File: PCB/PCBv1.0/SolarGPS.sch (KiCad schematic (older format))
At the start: 64 parts, among them J1 Conn_01x10_Female, J2 Solar1+, J3 GND, J4 Conn_02x05_Odd_Even, J5 Solar2+, J6 GND, J7 Screw_Terminal_01x01, U1 BQ25505, U2 MAX-M10Q, U3 MAX40200AUK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

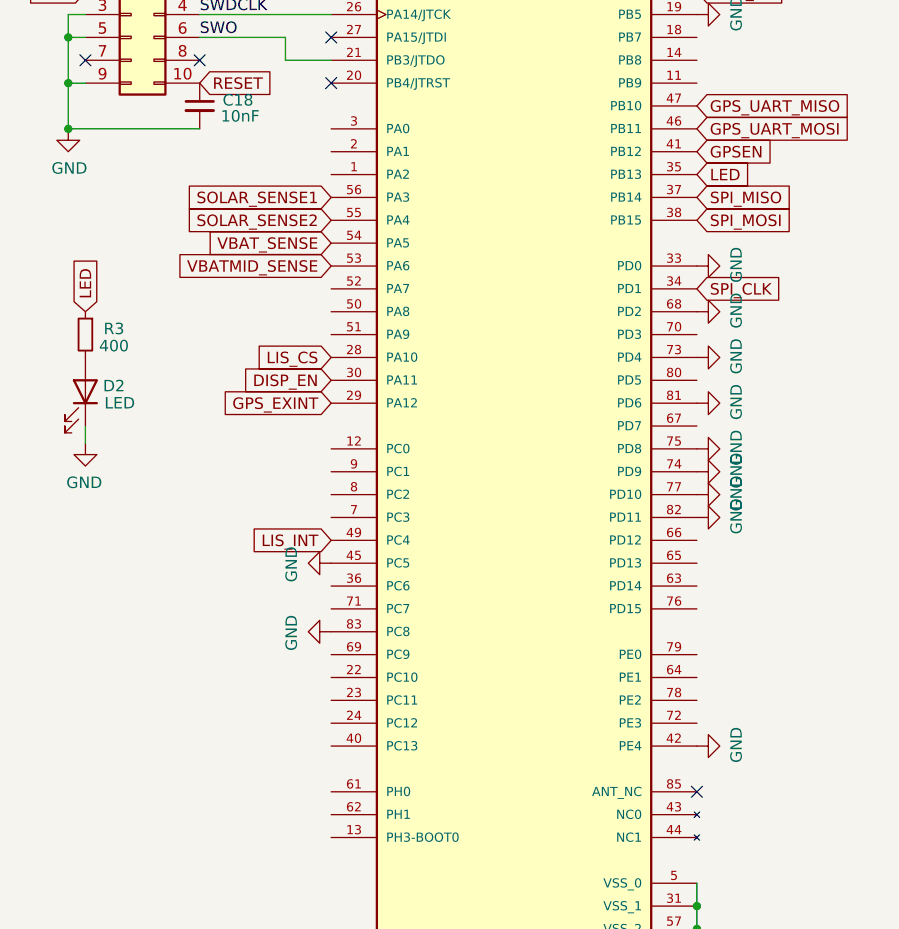
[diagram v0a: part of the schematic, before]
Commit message: Update PCB1.0 with new layout
Reverse the LCD direction for more space on the GPS signal
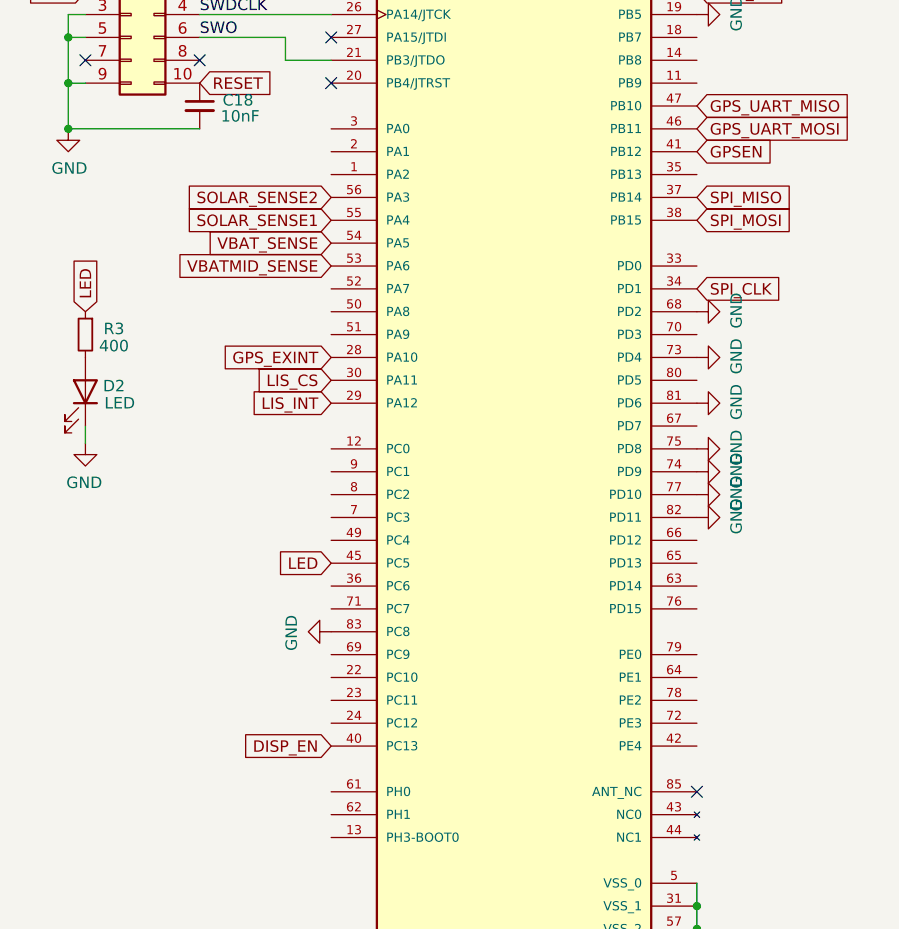
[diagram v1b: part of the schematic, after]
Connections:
- net DISP_EN: now also U4.40 (PC13); no longer U4.30 (PA11)
- net GND: no longer U4.33 (PD0), U4.42 (PE4), U4.45 (PC5)
- net GPS_EXINT: now also U4.28 (PA10); no longer U4.29 (PA12)
- net LED: now also U4.45 (PC5); no longer U4.35 (PB13)
- net LIS_CS: now also U4.30 (PA11); no longer U4.28 (PA10)
- net LIS_INT: now also U4.29 (PA12); no longer U4.49 (PC4)
- net SOLAR_SENSE1: now also U4.55 (PA4); no longer U4.56 (PA3)
- net SOLAR_SENSE2: now also U4.56 (PA3); no longer U4.55 (PA4)
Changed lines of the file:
@@
-$EndComp
-$Comp
-L power:GND #PWR0121
-U 1 1 61AA59EA
-P 10750 4475
-F 0 "#PWR0121" H 10750 4225 50  0001 C CNN
-F 1 "GND" H 10755 4302 50  0000 C CNN
-F 2 "" H 10750 4475 50  0001 C CNN
-F 3 "" H 10750 4475 50  0001 C CNN
-	1    10750 4475
-	0    1    1    0
 $EndComp
 $Comp
@@
 	1    9675 3725
 	0    1    -1   0
-$EndComp
-$Comp
-L power:GND #PWR0118
-U 1 1 61C248C7
-P 12350 2075
-F 0 "#PWR0118" H 12350 1825 50  0001 C CNN
-F 1 "GND" H 12355 1902 50  0000 C CNN
-F 2 "" H 12350 2075 50  0001 C CNN
-F 3 "" H 12350 2075 50  0001 C CNN
-	1    12350 2075
-	0    -1   -1   0
-$EndComp
-$Comp
-L power:GND #PWR0117
-U 1 1 61C22D24
-P 12350 3175
-F 0 "#PWR0117" H 12350 2925 50  0001 C CNN
-F 1 "GND" H 12355 3002 50  0000 C CNN
-F 2 "" H 12350 3175 50  0001 C CNN
-F 3 "" H 12350 3175 50  0001 C CNN
-	1    12350 3175
-	0    -1   -1   0
-$EndComp
-$Comp
-L power:GND #PWR0116
-U 1 1 61C21CD9
-P 12350 5275
-F 0 "#PWR0116" H 12350 5025 50  0001 C CNN
-F 1 "GND" H 12355 5102 50  0000 C CNN
-F 2 "" H 12350 5275 50  0001 C CNN
-F 3 "" H 12350 5275 50  0001 C CNN
-	1    12350 5275
-	0    -1   -1   0
 $EndComp
 $Comp
@@
 	1    0    0    -1
 $EndComp
-Text GLabel 10750 2975 0    50   Input ~ 0
+Text GLabel 10750 2875 0    50   Input ~ 0
 SOLAR_SENSE2
 Text GLabel 12350 2675 2    50   Input ~ 0
 GPSEN
-Text GLabel 10750 3675 0    50   Input ~ 0
+Text GLabel 10750 5275 0    50   Input ~ 0
 DISP_EN
 Text GLabel 12350 1975 2    50   Input ~ 0
@@
 Wire Wire Line
 	10175 1975 10750 1975
-Text GLabel 12350 2775 2    50   Input ~ 0
+Text GLabel 10750 4475 0    50   Input ~ 0
 LED
 Text GLabel 9675 3375 1    50   Input ~ 0
@@
 Text GLabel 12350 1875 2    50   Input ~ 0
 EXTCOMIN
-Text GLabel 10750 2875 0    50   Input ~ 0
+Text GLabel 10750 2975 0    50   Input ~ 0
 SOLAR_SENSE1
 Text GLabel 10750 3075 0    50   Input ~ 0
 VBAT_SENSE
-Text GLabel 10750 3775 0    50   Input ~ 0
+Text GLabel 10750 3575 0    50   Input ~ 0
 GPS_EXINT
 Text GLabel 12350 2575 2    50   Input ~ 0
@@
 Text GLabel 7450 3100 0    50   Input ~ 0
 LIS_CS
-Text GLabel 10750 3575 0    50   Input ~ 0
+Text GLabel 10750 3675 0    50   Input ~ 0
 LIS_CS
 Text GLabel 8050 2300 1    50   Input ~ 0
@@
 	1    0    0    -1
 $EndComp
-Text GLabel 10750 4375 0    50   Input ~ 0
+Text GLabel 10750 3775 0    50   Input ~ 0
 LIS_INT
 Text GLabel 12350 3275 2    50   Input ~ 0
@@
 DISP_EN
 $Comp
-L power:GND #PWR?
+L power:GND #PWR0128
 U 1 1 61C00045
 P 8775 5550
-F 0 "#PWR?" H 8775 5300 50  0001 C CNN
+F 0 "#PWR0128" H 8775 5300 50  0001 C CNN
 F 1 "GND" H 8780 5377 50  0000 C CNN
 F 2 "" H 8775 5550 50  0001 C CNN
@@
 Wire Notes Line
 	9275 6125 6725 6125
+$Comp
+L power:GND #PWR0116
+U 1 1 61B71588
+P 12350 2075
+F 0 "#PWR0116" H 12350 1825 50  0001 C CNN
+F 1 "GND" H 12355 1902 50  0000 C CNN
+F 2 "" H 12350 2075 50  0001 C CNN
+F 3 "" H 12350 2075 50  0001 C CNN
+	1    12350 2075
+	0    -1   -1   0
+$EndComp
 $EndSCHEMATC

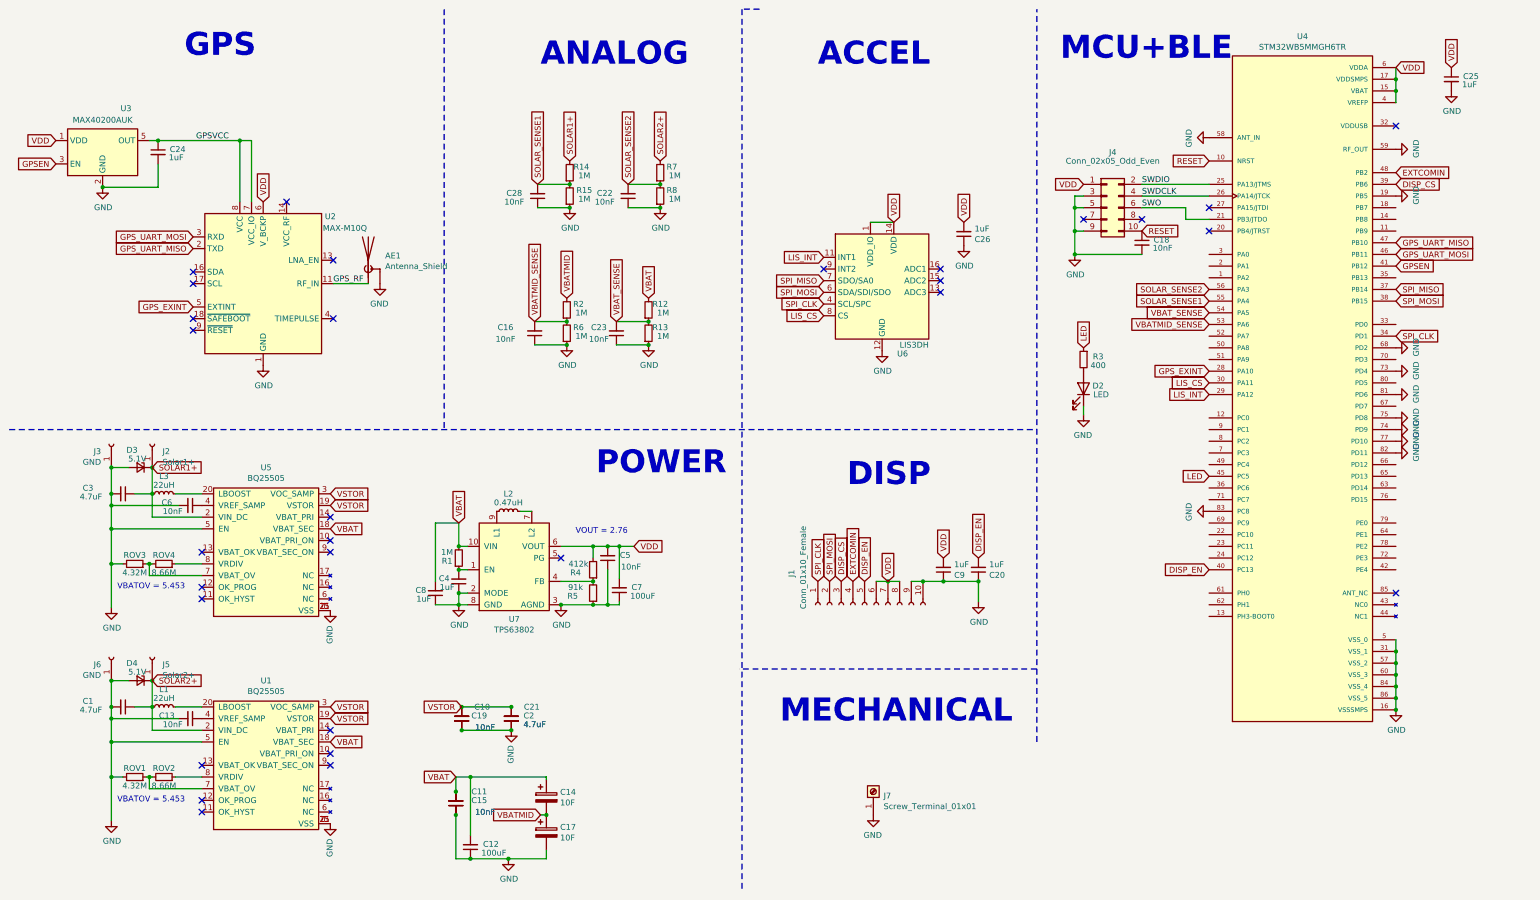
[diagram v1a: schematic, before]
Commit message: Cost reduction, remove second mppt
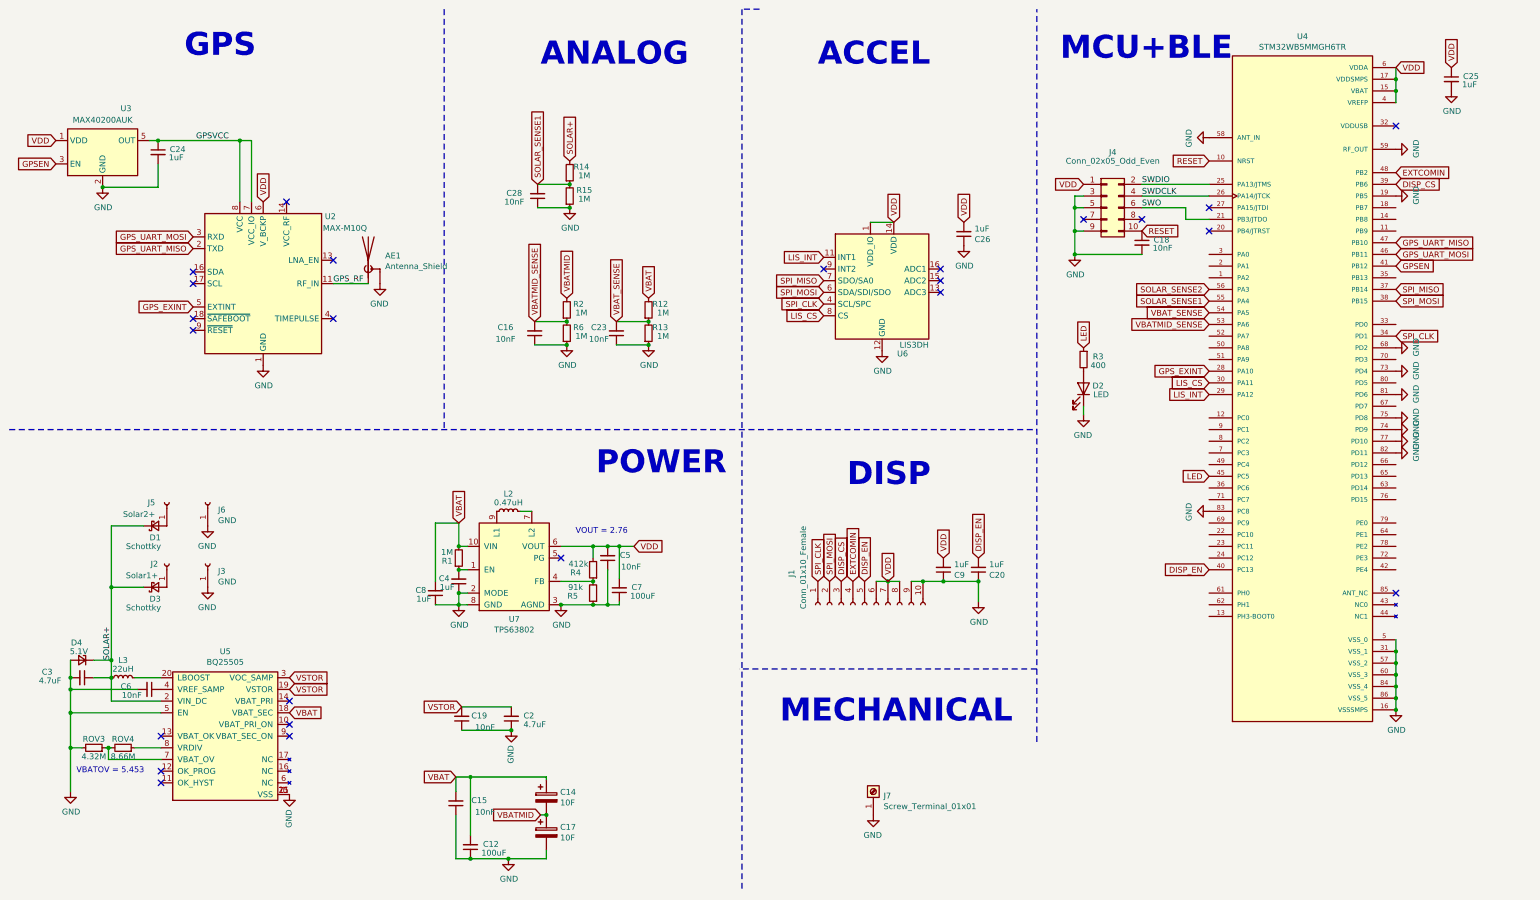
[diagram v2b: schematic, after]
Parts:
- removed C1, C21: 4.7uF, Capacitor_SMD:C_0805_2012Metric, symbol Device:C_Small
- removed C10, C11, C13, C22: 10nF, Capacitor_SMD:C_0603_1608Metric, symbol Device:C_Small
- removed D3: 5.1V, Diode_SMD:D_SOD-523, symbol Device:D_Zener_Small
- removed L1: 22uH, Inductor_SMD:L_1008_2520Metric, symbol Device:L_Small
- removed R7, R8: 1M, Resistor_SMD:R_0603_1608Metric, symbol Device:R_Small
- removed ROV1: 4.32M, Resistor_SMD:R_0603_1608Metric, symbol Device:R_Small
- removed ROV2: 8.66M, Resistor_SMD:R_0603_1608Metric, symbol Device:R_Small
- removed U1: BQ25505, Package_DFN_QFN:QFN-20-1EP_3.5x3.5mm_P0.5mm_EP2x2mm_ThermalVias, symbol MargoGeneral:BQ25505
- added D1, D3: Schottky, Diode_SMD:D_SOD-323_HandSoldering, symbol Device:D_Schottky_Small
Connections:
- net SOLAR1+ renamed SOLAR+
- net SOLAR+: now also D4.1 (K), D1.1 (K), D3.1 (K); no longer J2.1 (Pin_1)
- net SOLAR2+: no longer names the net of J5.1 (Pin_1)
- net SOLAR2+: now also D1.2 (A); no longer D4.1 (K)
- new net: D3.2 (A), J2.1 (Pin_1)
- no-connect marks 30 -> 24
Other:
- moved on the sheet: C3, C6, D4, J2, J3, J5, J6, L3, ROV3, ROV4, U5

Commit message: Update BOM, start treebuilders
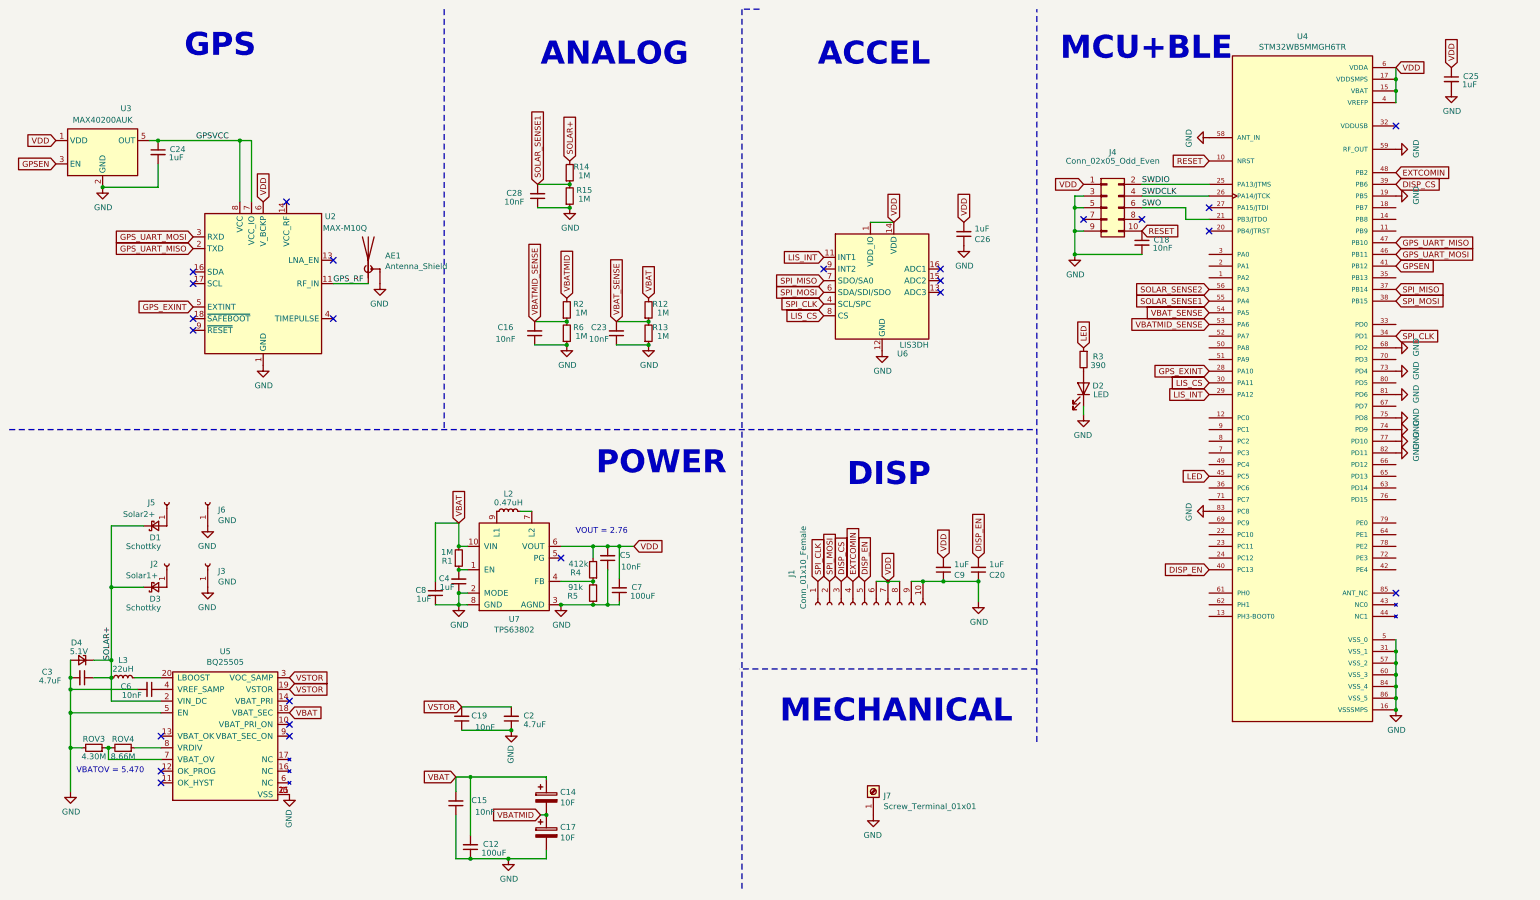
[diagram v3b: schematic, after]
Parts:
- D2: Part LTST-S270CKT -> LS R976-NR-1
- D4: Part (none) -> BZT52C5V1T-TP
- J4: Part (none) -> PM20C05VBDN
- L3: footprint Inductor_SMD:L_1008_2520Metric -> Inductor_SMD:L_1210_3225Metric; Part LPS4018-223M -> CBC3225T220MR
- R3: value 400 -> 390
- ROV3: value 4.32M -> 4.30M
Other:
- note added: "VBATOV = 5.470"
- note removed: "VBATOV = 5.453"
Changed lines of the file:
@@
 F 2 "Diode_SMD:D_SOD-523" V 1100 6050 50  0001 C CNN
 F 3 "~" V 1100 6050 50  0001 C CNN
+F 4 "BZT52C5V1T-TP" H 1100 6050 50  0001 C CNN "Part"
 	1    1100 6050
 	-1   0    0    -1
@@
 F 0 "L3" V 1600 6200 50  0000 C CNN
 F 1 "22uH" V 1525 6200 50  0000 C CNN
-F 2 "Inductor_SMD:L_1008_2520Metric" H 1450 6200 50  0001 C CNN
+F 2 "Inductor_SMD:L_1210_3225Metric" H 1450 6200 50  0001 C CNN
 F 3 "~" H 1450 6200 50  0001 C CNN
-F 4 "LPS4018-223M" V 1450 6200 50  0001 C CNN "Part"
+F 4 "CBC3225T220MR" V 1450 6200 50  0001 C CNN "Part"
 	1    1450 6200
 	0    -1   -1   0
@@
 P 1200 6800
 F 0 "ROV3" V 1275 6800 50  0000 C CNN
-F 1 "4.32M" V 1125 6800 50  0000 C CNN
+F 1 "4.30M" V 1125 6800 50  0000 C CNN
 F 2 "Resistor_SMD:R_0603_1608Metric" H 1200 6800 50  0001 C CNN
 F 3 "~" H 1200 6800 50  0001 C CNN
@@
 VSTOR
 Text Notes 1050 7025 0    50   ~ 0
-VBATOV = 5.453
+VBATOV = 5.470
 $Comp
 L MargoGeneral:BQ25505 U5
@@
 F 2 "Diode_SMD:D_0805_2012Metric" H 9675 3725 50  0001 C CNN
 F 3 "~" H 9675 3725 50  0001 C CNN
-F 4 "LTST-S270CKT" H 9675 3725 50  0001 C CNN "Part"
+F 4 "LS R976-NR-1" H 9675 3725 50  0001 C CNN "Part"
 	1    9675 3725
 	0    1    -1   0
@@
 P 9675 3475
 F 0 "R3" H 9550 3500 50  0000 C CNN
-F 1 "400" H 9550 3425 50  0000 C CNN
+F 1 "390" H 9550 3425 50  0000 C CNN
 F 2 "Resistor_SMD:R_0603_1608Metric" H 9675 3475 50  0001 C CNN
 F 3 "~" H 9675 3475 50  0001 C CNN
@@
 F 2 "Connector_PinHeader_2.00mm:PinHeader_2x05_P2.00mm_Vertical_SMD" H 9875 2175 50  0001 C CNN
 F 3 "~" H 9875 2175 50  0001 C CNN
+F 4 "PM20C05VBDN" H 9875 2175 50  0001 C CNN "Part"
 	1    9875 2175
 	1    0    0    -1
